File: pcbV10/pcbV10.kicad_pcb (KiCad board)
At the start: 2 copper layers, 100 x 100 mm, 146 parts, among them J1 PROG, J10 Fan1, J11 Fan2, J12 VPS, J13 SPK, J14 LoRa, J2 Servo, J3 I2C, J4 1wire, J5 EXT, J6 Power, J7 485, J8 POWER, J9 RGB, K1 G6K-2, K2 G6K-2, K3 G6K-2, Q1 BC817, Q2 BC817, Q3 AO3400A, Q4 BC817, Q5 IRLML6344, Q6 BC817, Q7 IRLML5203, Q8 IRF530, Q9 IRLML6344, SW1 BLUE, SW2 YELLOW, SW3 GREEN, SW4 RED, SW5 WHITE, U1 AMS1117-3.3, U10 SR602, U11 LM358, U12 DS18B20, U13 DS18B20, U14 IPS_240_240, U15 DS18B20, U16 MODULE_STEPDOWN, U17 RFM95W-868S2, U18 MD8002A, U19 BME280, U2 ESP32-WROOM-32, U20 CCS811, U3 CH340K, U4 MS4525DO, U5 INMP441_Module, U6 MAX3485, U7 BME680, U8 IP2721, U9 BH1750_Module, X1 FAN_6024

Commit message: pcb V10 as ordered at JLCPCB
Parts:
- removed D9: 10V, Diode_SMD:D_MiniMELF
- removed JP1: 485_TERM, Connector_PinHeader_2.54mm:PinHeader_1x02_P2.54mm_Vertical
- removed JP2: FAN 5V 24V, Connector_PinHeader_2.54mm:PinHeader_1x03_P2.54mm_Vertical
- removed Q6: BC817, Package_TO_SOT_SMD:SOT-23
- removed Q7: IRLML5203, Package_TO_SOT_SMD:SOT-23
- removed Q8: IRF530, Package_TO_SOT_THT:TO-220-3_Horizontal_TabDown
- removed R28, R29: 1k, Resistor_SMD:R_0603_1608Metric
- removed R30: 220R, Resistor_SMD:R_1206_3216Metric
- added C31: u1, Capacitor_SMD:C_0603_1608Metric, F.Cu at (83.9, 110.5)
- added C32: 10u, Capacitor_SMD:C_1206_3216Metric, F.Cu at (73.7, 99.4)
- added C33: u1, Capacitor_SMD:C_0805_2012Metric, F.Cu at (75.9, 98.9)
- added C34: u1, Capacitor_SMD:C_0603_1608Metric, F.Cu at (82.5, 98.9)
- added C35: u1, Capacitor_SMD:C_0603_1608Metric, F.Cu at (78.6, 102.2)
- added C36: 22u, Capacitor_SMD:C_0805_2012Metric, F.Cu at (71.1, 90.2)
- added C37: 22u, Capacitor_SMD:C_0805_2012Metric, F.Cu at (69.1, 90.2)
- added D16: Schttky, Diode_SMD:D_SMA, F.Cu at (79.8, 77.9)
- added FID1: Fiducial, Fiducial:Fiducial_1mm_Mask2mm, F.Cu at (55.2, 55.1)
- added FID2: Fiducial, Fiducial:Fiducial_1mm_Mask2mm, F.Cu at (120.0, 146.4)
- added IMG1: Speaker, liebler_DRAWINGS:speaker, F.Cu at (98.9, 93.0)
- added IMG2: Augenschutz, liebler_DRAWINGS:augenschutz, F.Cu at (85.6, 86.0)
- added IMG3: HOT, liebler_DRAWINGS:hot, F.Cu at (71.4, 56.3)
- added IMG4: WHS, liebler_DRAWINGS:LOGO_WHS, B.Cu at (119.4, 143.6)
- added IMG5: QR-CODE, liebler_DRAWINGS:QR_CODE_smopla_de, B.Cu at (84.7, 141.5)
- added IMG6: OPEN Hardware, Symbol:OSHW-Logo2_7.3x6mm_SilkScreen, B.Cu at (139.3, 56.6)
- added IMG7: HOT, liebler_DRAWINGS:hot, F.Cu at (127.6, 59.9)
- added IMG8: HOT_BIG, liebler_DRAWINGS:hot_big, B.Cu at (96.3, 87.1)
- added J15: 1B 2A, Connector_Phoenix_MC:PhoenixContact_MCV_1,5_2-G-3.81_1x02_P3.81mm_Vertical, F.Cu at (66.2, 111.0)
- added J16: BME280, Connector_PinSocket_2.54mm:PinSocket_1x06_P2.54mm_Vertical, F.Cu at (62.5, 132.0)
- added J17: CCS811, Connector_PinSocket_2.54mm:PinSocket_1x08_P2.54mm_Vertical, F.Cu at (138.7, 74.3)
- added J18: Barrel_Jack_Switch, Connector_BarrelJack:BarrelJack_Horizontal, F.Cu at (67.2, 60.7)
- added J19: Supply, Connector_PinHeader_2.54mm:PinHeader_2x04_P2.54mm_Vertical, F.Cu at (142.4, 65.3)
- added L1: 47u, Inductor_SMD:L_Abracon_ASPI-0630LR, F.Cu at (79.8, 72.5)
- added L2: 10uH, Inductor_SMD:L_Abracon_ASPI-0630LR, F.Cu at (77.0, 92.7)
- added MK1: ICS-43434, liebler_SEMICONDUCTORS:MIC_ICS-43434, F.Cu at (86.4, 109.9)
- added R41: M1, Resistor_SMD:R_0603_1608Metric, F.Cu at (61.1, 101.1)
- added R42: 2k2, Capacitor_SMD:C_0603_1608Metric, F.Cu at (103.1, 91.4)
- added R43: M1, Resistor_SMD:R_0603_1608Metric, F.Cu at (86.4, 113.0)
- added R44: 1k, Resistor_SMD:R_0603_1608Metric, F.Cu at (119.0, 128.8)
- added R45: 6k8, Resistor_SMD:R_0603_1608Metric, F.Cu at (83.8, 94.5)
- added R46: 39k, Resistor_SMD:R_0603_1608Metric, F.Cu at (82.3, 91.4)
- added R47: k47, Resistor_SMD:R_0603_1608Metric, F.Cu at (83.8, 91.4)
- added SW10: 5V FAN 24V, liebler_MECH:Switch_SS12D00, F.Cu at (62.0, 83.6)
- added SW11: 24V->5V, liebler_MECH:Switch_SS12D00, F.Cu at (69.8, 86.5)
- added SW12: RESET, Button_Switch_SMD:SW_Push_1P1T_NO_6x6mm_H9.5mm, F.Cu at (76.3, 129.9)
- added SW6: TERM ON, liebler_MECH:Switch_SS12D00, F.Cu at (78.0, 108.8)
- added SW7: LED HEATER, liebler_MECH:Switch_SS12D00, F.Cu at (102.0, 113.2)
- added SW8: REL ROT, liebler_MECH:Switch_SS12D00, F.Cu at (106.0, 122.2)
- added SW9: SNS MOV, liebler_MECH:Switch_SS12D00, F.Cu at (93.3, 113.2)
- added U21: BTS462T, Package_TO_SOT_SMD:TO-252-5_TabPin3, F.Cu at (65.7, 75.7)
- C17, C19: footprint Capacitor_SMD:C_0805_2012Metric -> Capacitor_SMD:C_1206_3216Metric
- C2: footprint Capacitor_SMD:C_0805_2012Metric -> Capacitor_SMD:C_0603_1608Metric
- C21: value u1 -> 1u; footprint Capacitor_SMD:C_0603_1608Metric -> Capacitor_SMD:C_1206_3216Metric
- C22: value 10n -> 10u; footprint Capacitor_SMD:C_0603_1608Metric -> Capacitor_SMD:C_1206_3216Metric
- D10, D11, D12, D13, D14: footprint liebler_OPTO:LED_PLCC_2835_Handsoldering -> liebler_OPTO:LED_PLCC_2835; moved to F.Cu
- D6, D7, D8: footprint LED_SMD:LED_PLCC_2835 -> liebler_OPTO:LED_PLCC_2835
- J1, J8: footprint Connector_USB:USB_C_Receptacle_HRO_TYPE-C-31-M-12 -> liebler_CONN:USB_C_Receptacle_HRO_TYPE-C-31-M-12_IMPROVED
- J12: footprint Connector_PinSocket_2.54mm:PinSocket_2x25_P2.54mm_Vertical -> Connector_PinHeader_2.54mm:PinHeader_2x25_P2.54mm_Vertical
- J13: footprint Connector_PinHeader_2.54mm:PinHeader_1x02_P2.54mm_Vertical -> Connector_Wire:SolderWire-0.1sqmm_1x02_P3.6mm_D0.4mm_OD1mm
- J14: value LoRa -> LoRa Antenna
- J6: value Power -> 5V 3V GN 24
- J9: value RGB -> GN 5V RGB GN
- R13: value 120R -> K12
- R26: value 22k -> 10k
- R27: value 1k -> 1M
- R31: value k1 -> 51k
- R32: value 1k -> 22R
- R33: value 1R -> R68
- RV1: value 5k -> 1k
- SW1: value BLUE -> BTN BLUE; footprint Button_Switch_SMD:SW_Push_1P1T_NO_CK_PTS125Sx43PSMTR -> liebler_MECH:SW_Push_1P1T_NO_CK_PTS125Sx43PSMTR
- SW3, SW4: footprint Button_Switch_SMD:SW_Push_1P1T_NO_CK_PTS125Sx43PSMTR -> liebler_MECH:SW_Push_1P1T_NO_CK_PTS125Sx43PSMTR
- SW5: value WHITE -> BTN WHITE; footprint Button_Switch_SMD:SW_Push_1P1T_NO_CK_PTS125Sx43PSMTR -> liebler_MECH:SW_Push_1P1T_NO_CK_PTS125Sx43PSMTR
- U11: value LM358 -> MP4420; footprint Package_SO:SO-8_3.9x4.9mm_P1.27mm -> Package_TO_SOT_SMD:TSOT-23-8
- U18, U6: footprint Package_SO:SO-8_3.9x4.9mm_P1.27mm -> Package_SO:SOIC-8_3.9x4.9mm_P1.27mm
- U5: value INMP441_Module -> ZXLD1350; footprint liebler_MODULES:INMP441_Module -> Package_TO_SOT_SMD:SOT-23-5
- U9: moved to F.Cu
- moved R19 66.1 mm to (126.4, 54.5)
- moved D6 62.0 mm to (127.4, 59.1), turned to 90 degrees
- moved U5 45.1 mm to (73.5, 72.5), turned to 270 degrees
- moved R26 34.7 mm to (85.3, 69.6)
- moved U9 34.4 mm to (112.4, 92.5), turned to 270 degrees
- moved C21 28.3 mm to (69.0, 70.9), turned to 0 degrees
- moved R33 24.0 mm to (73.6, 75.6), turned to 180 degrees
- moved R12 22.6 mm to (102.4, 103.6)
- moved R11 22.3 mm to (99.1, 107.2)
- moved D4 22.0 mm to (98.8, 104.6), turned to 90 degrees
- moved R8 18.8 mm to (66.0, 140.0), turned to 270 degrees
- moved R36 17.6 mm to (121.8, 124.5), turned to 90 degrees
- moved D11 16.3 mm to (86.1, 79.6), turned to 270 degrees
- moved R5 15.2 mm to (66.0, 143.1), turned to 90 degrees
- moved J7 14.4 mm to (75.1, 109.1), turned to 90 degrees
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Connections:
- C21 pad 1: +24V -> GND
- C21 pad 2: GND -> +24V
- C22 pad 1: Net-(C22-Pad1) -> GND
- C22 pad 2: Net-(C22-Pad2) -> +24V
- D14 pad 2: +24V -> Net-(D14-Pad2)
- J2 pad 1: 485_DI -> FAN1_DRIVE
- J2 pad 2: FAN1_SENSE -> SERVO2
- R27 pad 1: GND -> +24V
- R27 pad 2: Net-(R26-Pad1) -> Net-(R27-Pad2)
- R31 pad 1: Net-(C22-Pad2) -> Net-(R31-Pad1)
- R31 pad 2: Net-(Q8-Pad1) -> Net-(R31-Pad2)
- R32 pad 1: Net-(C22-Pad1) -> Net-(C35-Pad2)
- R32 pad 2: Net-(Q8-Pad3) -> Net-(R32-Pad2)
- R33 pad 1: Net-(Q8-Pad3) -> +24V
- R33 pad 2: GND -> Net-(D14-Pad2)
- RV1 pad 1: AUDIO -> Net-(R42-Pad2)
- U11 pad 1: Net-(C22-Pad2) -> Net-(U11-Pad1)
- U11 pad 2: Net-(C22-Pad1) -> +24V
- U11 pad 3: Net-(R26-Pad1) -> Net-(C35-Pad1)
- U11 pad 5: (no net) -> Net-(R32-Pad2)
- U11 pad 6: (no net) -> Net-(R27-Pad2)
- U11 pad 7: (no net) -> Net-(C34-Pad2)
- U11 pad 8: +24V -> Net-(R31-Pad2)
- U14 pad 6: SPI_IO1 -> SERVO2
- U17 pad 15: SPI_IO1 -> SERVO2
- U2 pad 14: HEATER -> HEATER_LED
- U2 pad 16: LED_WHITE_P -> I2S_SCK
- U2 pad 26: SPI_IO1 -> SERVO2
- U2 pad 28: FAN1_SENSE -> I2S_WS
- U2 pad 29: ROT_B -> I2S_SD
- U2 pad 6: K3_A1 -> I34
- U2 pad 7: MOVE -> I35
- U5 pad 1: GND -> Net-(L1-Pad2)
- U5 pad 2: 485_DE -> GND
- U5 pad 3: 485_RO -> Net-(R26-Pad1)
- U5 pad 4: 485_DI -> Net-(D14-Pad2)
- U5 pad 5: +3V3 -> +24V
- U8 pad 11: /VBUS -> Net-(R41-Pad2)
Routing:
- net SERVO2: track 0.00 -> 102.0 mm, vias 0 -> 2
- net Net-(D6-Pad1): track 92.1 -> 15.7 mm, vias 1 -> 0
- net 485_DI: track 108.7 -> 37.1 mm, vias 2 -> 0
- net SPI_IO1: track 64.3 -> 0.00 mm
- net +3V3: track 379.2 -> 435.8 mm, vias 4 -> 6
- net +24V: track 217.1 -> 185.5 mm, vias 2 -> 5
- net LED_WHITE_P: track 28.9 -> 57.1 mm
- net +5V: track 419.4 -> 393.1 mm, vias 3 -> 2
- net Net-(C36-Pad1): track 0.00 -> 22.5 mm
- net I35: track 0.00 -> 20.8 mm
- net I2S_SCK: track 0.00 -> 18.0 mm, vias 0 -> 2
- net ROT_B: track 34.3 -> 17.9 mm, vias 2 -> 1
- net HEATER: track 77.4 -> 63.1 mm
- net I2S_SD: track 0.00 -> 14.1 mm
- net FAN1_SENSE: track 68.9 -> 82.6 mm, vias 4 -> 2
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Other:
- board text added: "+"
- board text added: "-"
- board text added: "2021-11-25 klaus.liebler@w-hs.de Wissen, was praktisch zählt!"
- board text added: "24 NC B+"
- board text added: "3V 1W GN 5V"
- board text added: "3V GN SC SD GN"
- board text added: "3V3 GND 5V 5V"
- board text added: "3V3 GND SCL SDA NC NC"
- board text added: "A- B+"
- board text added: "FS F+ GND"
- board text added: "G3S1"
- board text added: "G3S2"
- board text added: "K1"
- board text added: "K2"
- board text added: "K3"
- board text added: "Microphone"
- board text added: "NC F+ F-"
- board text added: "NC GN A-"
- board text added: "Speaker"
- board text added: "TERM: for RS485-Termination LED HEATER: power LED or heating resistor @ io12 REL ROT: K3-A1 or rotary encoder @ io34 SNS MOV: fan1-sense or movement-sensor @ io35 24V->5V: activate 24V-to-5V converter 5V FAN 24V: select 24V or 5V for both fans"
- board text added: "TIME REL!"
- board text added: "USB-C PD 20V / 2A"
- board text added: "USB-C Programming"
- board text removed: "2021-09-04 klaus.liebler@w-hs.de Wissen, was praktisch zählt!"
- board text removed: "A- GN NC"
- board text removed: "B+ NC 24"

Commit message: labathome v11 as ordered @ JLCPCB
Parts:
- removed R40: 4k7, Resistor_SMD:R_0603_1608Metric
- removed R43: M1, Resistor_SMD:R_0603_1608Metric
- added C38: 1u, Capacitor_SMD:C_0603_1608Metric, F.Cu at (67.6, 140.0)
- added C39: u1, Capacitor_SMD:C_0603_1608Metric, F.Cu at (83.9, 110.5)
- added C40: 10u, Capacitor_SMD:C_0805_2012Metric_Pad1.18x1.45mm_HandSolder, B.Cu at (117.2, 65.7)
- added C41: u1, Capacitor_SMD:C_0805_2012Metric_Pad1.18x1.45mm_HandSolder, B.Cu at (117.2, 63.6)
- added DWM1: DWM1000, RF_Module:DWM1000, B.Cu at (105.2, 58.0)
- added IMG9: Augenschutz, liebler_DRAWINGS:qwiic, F.Cu at (67.5, 145.5)
- added J20: FAN5V, Connector_JST:JST_XH_B2B-XH-A_1x02_P2.50mm_Vertical, B.Cu at (54.7, 83.7)
- added J21: QWIIC, Connector_JST:JST_SH_SM04B-SRSS-TB_1x04-1MP_P1.00mm_Horizontal, F.Cu at (57.3, 139.3)
- added R28: 4k7, Resistor_SMD:R_0603_1608Metric, F.Cu at (66.2, 132.0)
- added R29: M1, Resistor_SMD:R_0603_1608Metric, F.Cu at (86.4, 113.0)
- added U22: SR602, liebler_MODULES:PIR_Sensor_SR602, F.Cu at (100.0, 67.0)
- C11, C13: footprint Capacitor_SMD:C_0603_1608Metric -> Capacitor_SMD:C_0805_2012Metric_Pad1.18x1.45mm_HandSolder; moved to B.Cu
- C30: value 1u -> u1
- D16: value Schttky -> D
- IMG2: footprint liebler_DRAWINGS:augenschutz -> liebler_DRAWINGS:googles
- J18: value Barrel_Jack_Switch -> Power
- JP3, JP4: value 1I2C_3SPI -> SPI-I2C
- L1: value 47u -> 68u
- R30: renamed from R42; footprint Capacitor_SMD:C_0603_1608Metric -> Resistor_SMD:R_0603_1608Metric
- R37: value 2k2 -> 2k2?
- R38, R39: footprint Capacitor_SMD:C_0603_1608Metric -> Resistor_SMD:R_0603_1608Metric
- SW11: value 24V->5V -> ON 24V->5V
- U1: value AMS1117-3.3 -> AMS1117
- U10: value SR602 -> MS4525DO; footprint liebler_MODULES:PIR_Sensor_SR602 -> liebler_MODULES:MS4525DO
- U12: value DS18B20 -> BME680; footprint Package_TO_SOT_THT:TO-92_HandSolder -> Package_LGA:Bosch_LGA-8_3x3mm_P0.8mm_ClockwisePinNumbering; moved to F.Cu
- U13: value DS18B20 -> BME280; footprint Package_TO_SOT_THT:TO-92_HandSolder -> Package_LGA:Bosch_LGA-8_2.5x2.5mm_P0.65mm_ClockwisePinNumbering
- U15: value DS18B20 -> CCS811; footprint Package_TO_SOT_THT:TO-92_HandSolder -> liebler_SEMICONDUCTORS:AMS_LGA-10-1EP_2.7x4mm_P0.6mm
- U19: value BME280 -> DS18B20; footprint Package_LGA:Bosch_LGA-8_2.5x2.5mm_P0.65mm_ClockwisePinNumbering -> Package_TO_SOT_THT:TO-92_HandSolder; moved to B.Cu
- U20: value CCS811 -> BH1750_Module; footprint liebler_SEMICONDUCTORS:AMS_LGA-10-1EP_2.7x4mm_P0.6mm -> liebler_MODULES:GY-302
- U4: value MS4525DO -> CH340C; footprint liebler_MODULES:MS4525DO -> Package_SO:SOIC-16_3.9x9.9mm_P1.27mm; moved to B.Cu
- U7: value BME680 -> DS18B20; footprint Package_LGA:Bosch_LGA-8_3x3mm_P0.8mm_ClockwisePinNumbering -> Package_TO_SOT_THT:TO-92_HandSolder
- U9: value BH1750_Module -> DS18B20; footprint liebler_MODULES:GY-302 -> Package_TO_SOT_THT:TO-92_HandSolder
- moved C15 100.3 mm to (72.7, 138.0), turned to 90 degrees
- moved U4 98.0 mm to (71.0, 128.4), turned to 270 degrees
- moved U12 86.7 mm to (70.0, 135.8), turned to 90 degrees
- moved U15 85.5 mm to (66.7, 136.2), turned to 0 degrees
- moved U19 84.0 mm to (124.5, 68.3), turned to 270 degrees
- moved C31 71.6 mm to (130.7, 56.3)
- moved U20 63.2 mm to (112.4, 92.5), turned to 270 degrees
- moved U7 56.8 mm to (125.7, 124.5)
- moved U13 53.3 mm to (73.5, 135.1)
- moved IMG5 45.4 mm to (75.9, 96.9)
- moved U10 40.2 mm to (139.2, 58.0)
- moved IMG4 39.8 mm to (129.7, 105.2), turned to 270 degrees
- moved U9 25.0 mm to (118.7, 68.3)
- moved IMG8 18.8 mm to (81.8, 75.2)
- moved C11 16.0 mm to (71.4, 123.6), turned to 180 degrees
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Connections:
- net Net-(C35-Pad1) renamed /psu/SW
- net Net-(D10-Pad1) renamed /D10_COOL
- net Net-(D10-Pad2) renamed /D12_COOL
- net Net-(D11-Pad1) renamed /D11_COOL
- net Net-(D12-Pad2) renamed /D14_COOL
- net Net-(D13-Pad1) renamed /D13_COOL
- C11 pad 2: +3V3 -> Net-(C11-Pad2)
- C13 pad 1: GND -> +5V
- C13 pad 2: +3V3 -> GND
- C15 pad 2: +5V -> +3V3
- C30 pad 1: +3V3 -> GND
- C30 pad 2: GND -> +3V3
- C31 pad 2: +3V3 -> +5V
- J1 pad A6: Net-(J1-PadA6) -> /UD+
- J1 pad A7: Net-(J1-PadA7) -> /UD-
- J1 pad B6: Net-(J1-PadA6) -> /UD+
- J1 pad B7: Net-(J1-PadA7) -> /UD-
- U10 pad 2: +3V3 -> +5V
- U10 pad 3: MOVE -> SDA
- U12 pad 2: 1wire -> +3V3
- U12 pad 3: +3V3 -> SDA
- U13 pad 2: 1wire -> +3V3
- U13 pad 3: +3V3 -> SDA
- U15 pad 2: 1wire -> Net-(R28-Pad1)
- U15 pad 3: +3V3 -> Net-(U15-Pad3)
- U19 pad 1: Net-(U19-Pad1) -> GND
- U19 pad 2: +3V3 -> 1wire
- U19 pad 3: SDA -> +3V3
- U2 pad 16: I2S_SCK -> I2S_WS
- U2 pad 28: I2S_WS -> I2S_SD
- U2 pad 29: I2S_SD -> I2S_SCK
- U20 pad 1: GND -> +3V3
- U20 pad 2: Net-(R40-Pad1) -> GND
- U20 pad 3: Net-(U20-Pad3) -> SCL
- U20 pad 4: Net-(U20-Pad4) -> SDA
- U20 pad 5: Net-(U20-Pad4) -> GND
- U3 pad 1: Net-(J1-PadA6) -> /UD+
- U3 pad 2: Net-(J1-PadA7) -> /UD-
- U4 pad 2: +5V -> PROG_TX
- U4 pad 3: SDA -> PROG_RX
- U4 pad 4: SCL -> Net-(C11-Pad2)
- U4 pad 5: Net-(U4-Pad5) -> /UD+
- U4 pad 6: Net-(U4-Pad6) -> /UD-
- U7 pad 2: +3V3 -> 1wire
- U7 pad 3: SDA -> +3V3
- U9 pad 1: +3V3 -> GND
- U9 pad 2: GND -> 1wire
- U9 pad 3: SCL -> +3V3
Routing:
- net GND: track 63.2 -> 98.2 mm, vias 167 -> 160
- net /UD-: track 0.00 -> 24.5 mm, vias 0 -> 1
- net /UD+: track 0.00 -> 23.9 mm, vias 0 -> 2
- net +5V: track 393.1 -> 415.7 mm, vias 2 -> 3
- net +3V3: track 435.8 -> 456.9 mm
- net Net-(J1-PadA6): track 10.6 -> 0.00 mm, vias 2 -> 0
- net SPI_MISO: track 88.5 -> 97.5 mm
- net PROG_RX: track 24.2 -> 33.2 mm
- net SDA: track 184.2 -> 192.8 mm
- net Net-(J1-PadA7): track 7.53 -> 0.00 mm
- net /DTR: track 9.66 -> 16.5 mm, vias 0 -> 1
- net /RTS: track 3.18 -> 9.95 mm, vias 0 -> 1
- net Net-(J11-Pad2): track 30.3 -> 23.7 mm
- net SCL: track 168.3 -> 174.4 mm, vias 4 -> 5
- net I2S_WS: track 12.6 -> 18.0 mm, vias 0 -> 2
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- added copper zone on B.Cu, net /D10_COOL
- added copper zone on F.Cu, net /D10_COOL
- added copper zone on B.Cu, net /D11_COOL
- added copper zone on F.Cu, net /D11_COOL
- added copper zone on B.Cu, net /D12_COOL
- added copper zone on F.Cu, net /D12_COOL
- added copper zone on B.Cu, net /D13_COOL
- added copper zone on F.Cu, net /D13_COOL
- added copper zone on B.Cu, net /D14_COOL
- added copper zone on F.Cu, net /D14_COOL
- added copper zone on F.Cu, net /psu/SW
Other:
- board text added: "2021-12-22 Klaus Liebler"
- board text added: "F2 5V"
- board text added: "G5S1"
- board text added: "G5S2"
- board text added: "Micro"
- board text added: "TERM: for RS485-Termination LED HEATER: power LED or heating-R@ io12 REL ROT: K3-A1 or rotary encoder @ io34 SNS MOV: fan1- or movem.-sensor @ io35 24V->5V: activate 24V-to-5V converter 5V FAN 24V: select 24V or 5V for both fans"
- board text added: "für K., J. & S."
- board text added: "lab@home 11"
- board text removed: "-F2 +F2 NC"
- board text removed: "2021-11-25 klaus.liebler@w-hs.de Wissen, was praktisch zählt!"
- board text removed: "G3S1"
- board text removed: "G3S2"
- board text removed: "Microphone"
- board text removed: "TERM: for RS485-Termination LED HEATER: power LED or heating resistor @ io12 REL ROT: K3-A1 or rotary encoder @ io34 SNS MOV: fan1-sense or movement-sensor @ io35 24V->5V: activate 24V-to-5V converter 5V FAN 24V: select 24V or 5V for both fans"
- board text removed: "lab@home 10"

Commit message: Moved all components to esp-idf components repository
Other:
- board text added: "PullDown für LED Alle 0805 auf 0603-Fähigkeit prüfen Fiducials in Stencil Freistellung für UWB-Modul"

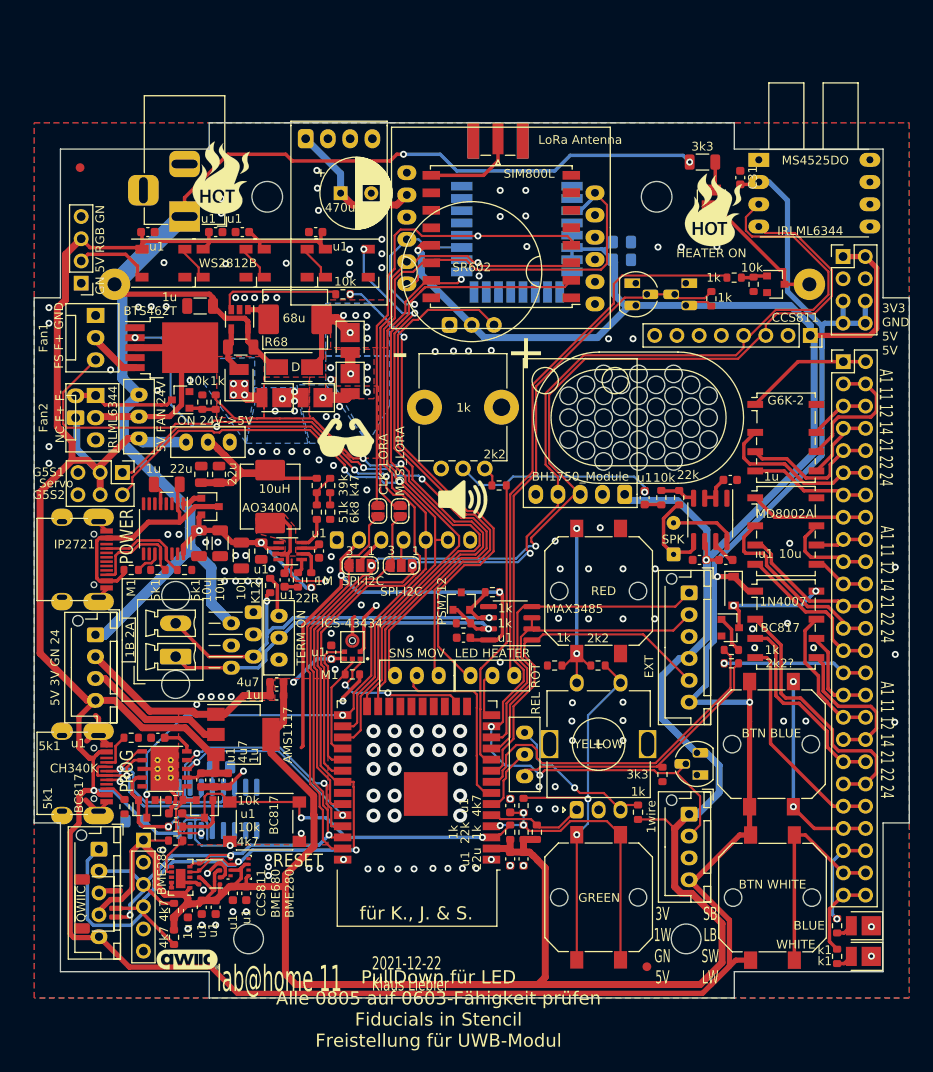
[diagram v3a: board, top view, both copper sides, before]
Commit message: All SMD components orderable @ JLCPCB
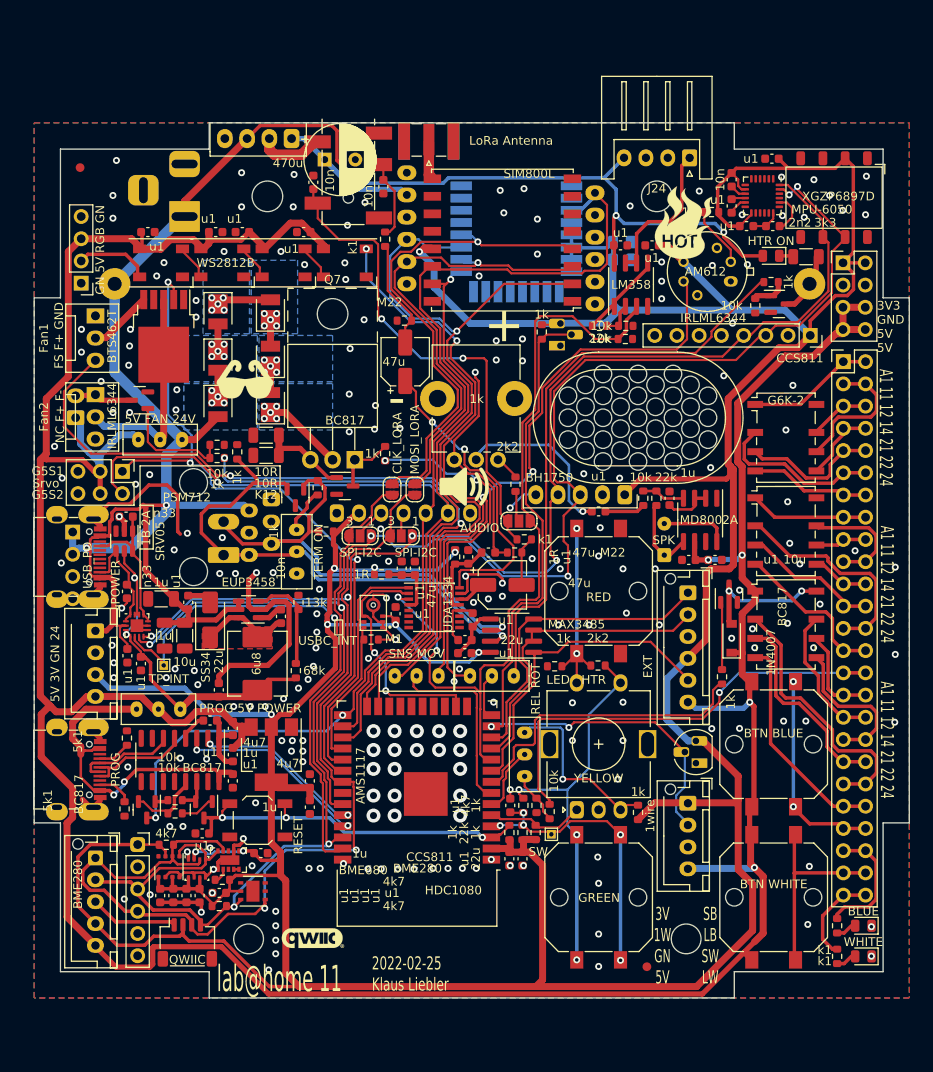
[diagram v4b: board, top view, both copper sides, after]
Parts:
- removed C21: 1u, Capacitor_SMD:C_1206_3216Metric
- removed C34: u1, Capacitor_SMD:C_0603_1608Metric
- removed C37: 22u, Capacitor_SMD:C_0805_2012Metric
- removed IMG3: HOT, liebler_DRAWINGS:hot
- removed L1: 68u, Inductor_SMD:L_Abracon_ASPI-0630LR
- removed MK1: ICS-43434, liebler_SEMICONDUCTORS:MIC_ICS-43434
- removed Q3: AO3400A, Package_TO_SOT_SMD:SOT-23
- removed R10, R9: 5k1, Resistor_SMD:R_0603_1608Metric
- removed R27: 1M, Resistor_SMD:R_0603_1608Metric
- removed R31: 51k, Resistor_SMD:R_0603_1608Metric
- removed R41: M1, Resistor_SMD:R_0603_1608Metric
- removed R47: k47, Resistor_SMD:R_0603_1608Metric
- added C42: u1, Capacitor_SMD:C_0603_1608Metric, F.Cu at (99.6, 99.6)
- added C43: 47u, Capacitor_SMD:C_0603_1608Metric, F.Cu at (101.9, 99.1)
- added C44: u1, Capacitor_SMD:C_0603_1608Metric, F.Cu at (100.1, 106.8)
- added C45: 47u, Capacitor_SMD:CP_Elec_5x5.4, F.Cu at (103.5, 102.8)
- added C46: 47u, Capacitor_SMD:CP_Elec_5x5.4, F.Cu at (92.4, 77.3)
- added C47: 22u, Capacitor_SMD:C_0603_1608Metric, F.Cu at (99.2, 109.1)
- added C48: 10n, Capacitor_SMD:C_0603_1608Metric, F.Cu at (81.9, 56.8)
- added C49: 10n, Capacitor_SMD:C_0603_1608Metric, F.Cu at (89.9, 57.3)
- added C50: 10n, Capacitor_SMD:C_0603_1608Metric, F.Cu at (129.7, 56.5)
- added C51: u1, Capacitor_SMD:C_0603_1608Metric, F.Cu at (129.7, 59.5)
- added C52: u1, Capacitor_SMD:C_0603_1608Metric, F.Cu at (131.4, 61.8)
- added C53: 2n2, Capacitor_SMD:C_0603_1608Metric, F.Cu at (134.4, 61.8)
- added C54: u1, Capacitor_SMD:C_0603_1608Metric, F.Cu at (117.0, 64.0)
- added C55: u1, Capacitor_SMD:C_0603_1608Metric, F.Cu at (120.6, 64.0)
- added C56: n33, Capacitor_SMD:C_0603_1608Metric, F.Cu at (60.5, 95.0)
- added C57: n33, Capacitor_SMD:C_0603_1608Metric, F.Cu at (60.6, 103.5)
- added C58: 1u, Capacitor_SMD:C_1206_3216Metric, F.Cu at (64.5, 104.4)
- added C59: u1, Capacitor_SMD:C_0603_1608Metric, F.Cu at (71.2, 138.0)
- added D9: WHITE, liebler_OPTO:LED_PLCC_2835, F.Cu at (77.0, 82.2)
- added J22: AudioJack3_SwitchT, liebler_CONN:PJ-327A, F.Cu at (85.9, 49.6)
- added J23: USB_PD, Connector_PinHeader_2.54mm:PinHeader_1x04_P2.54mm_Vertical, F.Cu at (54.4, 96.8)
- added J24: AOUT, Connector_JST:JST_XH_S4B-XH-A_1x04_P2.50mm_Horizontal, F.Cu at (124.9, 54.0)
- added JP1: AUDIO, Jumper:SolderJumper-3_P1.3mm_Open_RoundedPad1.0x1.5mm_NumberLabels, F.Cu at (105.4, 95.5)
- added JP2: USBC_INT, liebler_CONN:Jumper_Trace_025x150x015, F.Cu at (84.8, 107.7)
- added Q6: BC817, Package_TO_SOT_SMD:SOT-23, F.Cu at (85.5, 91.5)
- added Q7: TIP41, Package_TO_SOT_THT:TO-220-3_Horizontal_TabUp, F.Cu at (86.6, 88.5)
- added R40: 1R, Resistor_SMD:R_0603_1608Metric, F.Cu at (89.7, 101.6)
- added R42: 1R, Resistor_SMD:R_0603_1608Metric, F.Cu at (98.1, 99.6)
- added R43: M22, Resistor_SMD:R_0603_1608Metric, F.Cu at (104.9, 99.1)
- added R48: M22, Resistor_SMD:R_0603_1608Metric, F.Cu at (92.3, 72.6)
- added R49: k1, Resistor_SMD:R_0603_1608Metric, F.Cu at (106.0, 97.6)
- added R50: k1, Resistor_SMD:R_0603_1608Metric, F.Cu at (90.1, 63.3)
- added R51: 10k, Resistor_SMD:R_0603_1608Metric, F.Cu at (117.6, 73.2)
- added R52: 10k, Resistor_SMD:R_0603_1608Metric, F.Cu at (117.5, 74.7)
- added R53: 22k, Resistor_SMD:R_0603_1608Metric, F.Cu at (114.6, 73.2)
- added R54: 1M, Resistor_SMD:R_0603_1608Metric, F.Cu at (127.4, 60.2)
- added TP1: TP_INT, TestPoint:TestPoint_THTPad_1.0x1.0mm_Drill0.5mm, F.Cu at (64.8, 112.0)
- added TP2: SW, TestPoint:TestPoint_THTPad_1.0x1.0mm_Drill0.5mm, F.Cu at (109.1, 131.3)
- added U23: MPU-6050, Sensor_Motion:InvenSense_QFN-24_4x4mm_P0.5mm, F.Cu at (133.2, 58.4)
- added U24: SRV05, Package_TO_SOT_SMD:SOT-23-6, F.Cu at (60.3, 97.8)
- added X2: XGZP6897D, liebler_MODULES:XGZP6897D, F.Cu at (141.4, 58.5)
- C11: footprint Capacitor_SMD:C_0805_2012Metric_Pad1.18x1.45mm_HandSolder -> Capacitor_SMD:C_0603_1608Metric; moved to F.Cu
- C13: value u1 -> 47u; footprint Capacitor_SMD:C_0805_2012Metric_Pad1.18x1.45mm_HandSolder -> Capacitor_SMD:C_0603_1608Metric; moved to F.Cu
- C19, C32: value 10u -> u1; footprint Capacitor_SMD:C_1206_3216Metric -> Capacitor_SMD:C_0603_1608Metric
- C33, C36: footprint Capacitor_SMD:C_0805_2012Metric -> Capacitor_SMD:C_0603_1608Metric
- C35: value u1 -> 10n
- D16: value D -> SS34
- D6: value HEATER ON -> HTR ON; footprint liebler_OPTO:LED_PLCC_2835 -> LED_SMD:LED_0805_2012Metric
- D7, D8: footprint liebler_OPTO:LED_PLCC_2835 -> Diode_SMD:D_0805_2012Metric
- J2: value Servo -> Srvo
- L2: value 10uH -> 6u8
- R26: value 10k -> 1k
- R32: value 22R -> 10R; footprint Resistor_SMD:R_0603_1608Metric -> Resistor_SMD:R_1206_3216Metric
- R33: value R68 -> 10R
- R36: value 3k3 -> 1k
- R37: value 2k2? -> 10k
- R45: value 6k8 -> 13k
- R46: value 39k -> 68k
- RV1: footprint Potentiometer_THT:Potentiometer_Alps_RK09K_Single_Vertical -> liebler_MECH:Potentiometer_Alps_RK09K_Single_Vertical
- SW11: value ON 24V->5V -> PROG 5V POWER
- SW12: footprint Button_Switch_SMD:SW_Push_1P1T_NO_6x6mm_H9.5mm -> Button_Switch_SMD:SW_SPST_TL3342
- SW7: value LED HEATER -> LED HTR
- U10: value MS4525DO -> LM358; footprint liebler_MODULES:MS4525DO -> Package_SO:SOIC-8_3.9x4.9mm_P1.27mm
- U11: value MP4420 -> FUSB302BMPX; footprint Package_TO_SOT_SMD:TSOT-23-8 -> Package_DFN_QFN:WQFN-14-1EP_2.5x2.5mm_P0.5mm_EP1.45x1.45mm
- U20: value BH1750_Module -> BH1750
- U22: value SR602 -> AM612; footprint liebler_MODULES:PIR_Sensor_SR602 -> liebler_SEMICONDUCTORS:AM612
- U3: value CH340K -> ICS-43432; footprint liebler_SEMICONDUCTORS:SSOP-10_3.9x4.9mm_P1.00mm_EP -> liebler_SEMICONDUCTORS:MIC_ICS-43432
- U4: moved to F.Cu
- U5: value ZXLD1350 -> UDA1334; footprint Package_TO_SOT_SMD:SOT-23-5 -> Package_SO:SSOP-16_4.4x5.2mm_P0.65mm
- U8: value IP2721 -> HDC1080; footprint Package_SO:TSSOP-16_4.4x5mm_P0.65mm -> Package_SON:Texas_PWSON-N6
- U9: value DS18B20 -> EUP3458; footprint Package_TO_SOT_THT:TO-92_HandSolder -> Package_TO_SOT_SMD:SOT-23-6
- moved U9 57.9 mm to (74.5, 105.6), turned to 180 degrees
- moved IMG5 47.5 mm to (33.2, 76.3)
- moved C13 43.1 mm to (93.5, 100.9), turned to -90 degrees
- moved U8 42.7 mm to (75.0, 137.8), turned to 180 degrees
- moved U5 39.7 mm to (95.7, 105.4), turned to 0 degrees
- moved R11 32.4 mm to (73.2, 87.6), turned to 90 degrees
- moved SW11 31.0 mm to (64.2, 117.0), turned to 180 degrees
- moved C11 30.7 mm to (92.0, 100.9), turned to -90 degrees
- moved D16 30.5 mm to (70.1, 106.8), turned to 90 degrees
- moved U3 29.8 mm to (88.8, 106.0), turned to 180 degrees
- moved U22 26.9 mm to (126.9, 67.0)
- moved R37 26.8 mm to (108.9, 128.7), turned to 90 degrees
- moved C36 24.6 mm to (71.1, 114.8)
- moved U10 23.4 mm to (118.2, 68.5), turned to 90 degrees
- moved D4 22.4 mm to (79.8, 92.8), turned to -90 degrees
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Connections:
- C13 pad 1: +5V -> GND
- C13 pad 2: GND -> Net-(C11-Pad2)
- C17 pad 1: GND -> +24V
- C17 pad 2: /VBUS -> GND
- C19 pad 1: +24V -> GND
- C19 pad 2: GND -> /psu/5Vx
- C25 pad 1: +3V3 -> +5V
- C26 pad 1: +3V3 -> +5V
- C31 pad 2: +5V -> +3V3
- C35 pad 1: /psu/SW -> Net-(C35-Pad1)
- C35 pad 2: Net-(C35-Pad2) -> /psu/SW
- C36 pad 1: Net-(C36-Pad1) -> /psu/5Vx
- C6 pad 1: GND -> +5P
- C6 pad 2: +5V -> GND
- D14 pad 2: Net-(D14-Pad2) -> +24V
- D16 pad 1: +24V -> /psu/SW
- D16 pad 2: /D13_COOL -> GND
- D4 pad 1: RS485B -> RS485A
- D4 pad 2: RS485A -> RS485B
- D6 pad 2: Net-(D6-Pad2) -> +24V
- DWM1 pad 1: Net-(DWM1-Pad1) -> unconnected-(DWM1-Pad1)
- DWM1 pad 10: Net-(DWM1-Pad10) -> unconnected-(DWM1-Pad10)
- DWM1 pad 11: Net-(DWM1-Pad11) -> unconnected-(DWM1-Pad11)
- DWM1 pad 12: Net-(DWM1-Pad12) -> unconnected-(DWM1-Pad12)
- DWM1 pad 13: Net-(DWM1-Pad13) -> unconnected-(DWM1-Pad13)
- DWM1 pad 14: Net-(DWM1-Pad14) -> unconnected-(DWM1-Pad14)
- DWM1 pad 15: Net-(DWM1-Pad15) -> unconnected-(DWM1-Pad15)
- DWM1 pad 22: Net-(DWM1-Pad22) -> unconnected-(DWM1-Pad22)
- DWM1 pad 4: Net-(DWM1-Pad4) -> unconnected-(DWM1-Pad4)
- DWM1 pad 9: Net-(DWM1-Pad9) -> unconnected-(DWM1-Pad9)
- GSM_Module1 pad 1: Net-(GSM_Module1-Pad1) -> unconnected-(GSM_Module1-Pad1)
- GSM_Module1 pad 10: Net-(GSM_Module1-Pad10) -> unconnected-(GSM_Module1-Pad10)
- GSM_Module1 pad 11: Net-(GSM_Module1-Pad11) -> unconnected-(GSM_Module1-Pad11)
- GSM_Module1 pad 12: Net-(GSM_Module1-Pad12) -> unconnected-(GSM_Module1-Pad12)
- GSM_Module1 pad 3: Net-(GSM_Module1-Pad3) -> unconnected-(GSM_Module1-Pad3)
- GSM_Module1 pad 8: Net-(GSM_Module1-Pad8) -> unconnected-(GSM_Module1-Pad8)
- GSM_Module1 pad 9: Net-(GSM_Module1-Pad9) -> unconnected-(GSM_Module1-Pad9)
- J1 pad A4: +5V -> +5P
- J1 pad A8: Net-(J1-PadA8) -> unconnected-(J1-PadA8)
- J1 pad A9: +5V -> +5P
- J1 pad B4: +5V -> +5P
- J1 pad B8: Net-(J1-PadB8) -> unconnected-(J1-PadB8)
- J1 pad B9: +5V -> +5P
- J11 pad 3: Net-(J11-Pad3) -> unconnected-(J11-Pad3)
- J16 pad 5: Net-(J16-Pad5) -> unconnected-(J16-Pad5)
- J16 pad 6: Net-(J16-Pad6) -> unconnected-(J16-Pad6)
- J17 pad 6: Net-(J17-Pad6) -> unconnected-(J17-Pad6)
- J17 pad 7: Net-(J17-Pad7) -> unconnected-(J17-Pad7)
- J17 pad 8: Net-(J17-Pad8) -> unconnected-(J17-Pad8)
- J7 pad 1: Net-(J7-Pad1) -> unconnected-(J7-Pad1)
- J7 pad 4: Net-(J7-Pad4) -> unconnected-(J7-Pad4)
- J8 pad A4: /VBUS -> +24V
- J8 pad A5: Net-(J8-PadA5) -> /psu/CC1
- J8 pad A6: Net-(J8-PadA6) -> unconnected-(J8-PadA6)
- J8 pad A7: Net-(J8-PadA7) -> unconnected-(J8-PadA7)
- J8 pad A8: Net-(J8-PadA8) -> unconnected-(J8-PadA8)
- J8 pad A9: /VBUS -> +24V
- J8 pad B4: /VBUS -> +24V
- J8 pad B5: Net-(J8-PadB5) -> /psu/CC2
- J8 pad B6: Net-(J8-PadB6) -> unconnected-(J8-PadB6)
- J8 pad B7: Net-(J8-PadB7) -> unconnected-(J8-PadB7)
- J8 pad B8: Net-(J8-PadB8) -> unconnected-(J8-PadB8)
- J8 pad B9: /VBUS -> +24V
- L2 pad 1: Net-(C36-Pad1) -> /psu/5Vx
- Q5 pad 3: Net-(D6-Pad1) -> Net-(Q5-Pad3)
- R18 pad 2: Net-(D6-Pad1) -> Net-(Q5-Pad3)
- R19 pad 1: +24V -> Net-(D6-Pad1)
- R19 pad 2: Net-(D6-Pad2) -> Net-(Q5-Pad3)
- R26 pad 1: Net-(R26-Pad1) -> Net-(Q6-Pad3)
- R29 pad 1: GND -> I2S_SD
- R29 pad 2: I2S_SD -> GND
- R30 pad 1: AUDIO -> Net-(JP1-Pad2)
- R32 pad 1: Net-(C35-Pad2) -> Net-(Q6-Pad1)
- R32 pad 2: Net-(R32-Pad2) -> GND
- R33 pad 1: +24V -> Net-(Q6-Pad1)
- R33 pad 2: Net-(D14-Pad2) -> GND
- R46 pad 1: Net-(C36-Pad1) -> /psu/5Vx
- R46 pad 2: Net-(R31-Pad1) -> Net-(R45-Pad2)
- SW11 pad 1: +5V -> /psu/5Vx
- SW11 pad 2: Net-(C36-Pad1) -> +5V
- SW11 pad 3: Net-(SW11-Pad3) -> +5P
- SW6 pad 1: Net-(SW6-Pad1) -> unconnected-(SW6-Pad1)
- U10 pad 1: GND -> Net-(R53-Pad1)
- U10 pad 2: +5V -> Net-(R51-Pad2)
- U10 pad 3: SDA -> AUDIO
- U10 pad 4: SCL -> GND
- U10 pad 5: Net-(U10-Pad5) -> Net-(R53-Pad1)
- U10 pad 6: Net-(U10-Pad6) -> Net-(J24-Pad1)
- U10 pad 7: Net-(U10-Pad7) -> Net-(J24-Pad1)
- U10 pad 8: Net-(U10-Pad8) -> +24V
- U11 pad 1: Net-(U11-Pad1) -> /psu/CC2
- U11 pad 3: /psu/SW -> /psu/5Vx
- U11 pad 4: GND -> /psu/5Vx
- U11 pad 5: Net-(R32-Pad2) -> Net-(JP2-Pad2)
- U11 pad 6: Net-(R27-Pad2) -> SCL
- U11 pad 7: Net-(C34-Pad2) -> SDA
- U11 pad 8: Net-(R31-Pad2) -> GND
- U14 pad 7: Net-(U14-Pad7) -> unconnected-(U14-Pad7)
- U15 pad 3: Net-(U15-Pad3) -> unconnected-(U15-Pad3)
- U15 pad 8: Net-(U15-Pad8) -> unconnected-(U15-Pad8)
- U16 pad 2: Net-(U16-Pad2) -> GND
- U16 pad 3: Net-(U16-Pad3) -> +24V
- U16 pad 4: Net-(U16-Pad4) -> unconnected-(U16-Pad4)
- U17 pad 11: Net-(U17-Pad11) -> unconnected-(U17-Pad11)
- U17 pad 12: Net-(U17-Pad12) -> unconnected-(U17-Pad12)
- U17 pad 16: Net-(U17-Pad16) -> unconnected-(U17-Pad16)
- U17 pad 6: Net-(U17-Pad6) -> unconnected-(U17-Pad6)
- U17 pad 7: Net-(U17-Pad7) -> unconnected-(U17-Pad7)
- U18 pad 6: +3V3 -> +5V
- U2 pad 17: Net-(U2-Pad17) -> unconnected-(U2-Pad17)
- U2 pad 18: Net-(U2-Pad18) -> unconnected-(U2-Pad18)
- U2 pad 19: Net-(U2-Pad19) -> unconnected-(U2-Pad19)
- U2 pad 20: Net-(U2-Pad20) -> unconnected-(U2-Pad20)
- U2 pad 21: Net-(U2-Pad21) -> unconnected-(U2-Pad21)
- U2 pad 22: Net-(U2-Pad22) -> unconnected-(U2-Pad22)
- U2 pad 32: Net-(U2-Pad32) -> unconnected-(U2-Pad32)
- U22 pad 2: +3V3 -> Net-(R54-Pad2)
- U22 pad 3: MOVE -> GND
- U3 pad 1: /UD+ -> GND
- U3 pad 2: /UD- -> GND
- U3 pad 3: GND -> +3V3
- U3 pad 4: /DTR -> GND
- U3 pad 5: Net-(U3-Pad5) -> I2S_WS
- U3 pad 6: /RTS -> I2S_SCK
- U3 pad 7: +5V -> I2S_SD
- U4 pad 10: Net-(U4-Pad10) -> unconnected-(U4-Pad10)
- U4 pad 11: Net-(U4-Pad11) -> unconnected-(U4-Pad11)
- U4 pad 12: Net-(U4-Pad12) -> unconnected-(U4-Pad12)
- U4 pad 15: Net-(U4-Pad15) -> unconnected-(U4-Pad15)
- U4 pad 16: +5V -> +5P
- U4 pad 4: Net-(C11-Pad2) -> Net-(C10-Pad1)
- U4 pad 7: Net-(U4-Pad7) -> unconnected-(U4-Pad7)
- U4 pad 8: Net-(U4-Pad8) -> unconnected-(U4-Pad8)
- U4 pad 9: Net-(U4-Pad9) -> unconnected-(U4-Pad9)
- U5 pad 1: Net-(L1-Pad2) -> I2S_SCK
- U5 pad 2: GND -> I2S_WS
- U5 pad 3: Net-(R26-Pad1) -> AUDIO
- U5 pad 4: Net-(D14-Pad2) -> Net-(C11-Pad2)
- U5 pad 5: +24V -> GND
- U8 pad 1: Net-(Q3-Pad1) -> SDA
- U8 pad 2: /VBUS -> GND
- U8 pad 3: (no net) -> unconnected-(U8-Pad3)
- U8 pad 4: (no net) -> unconnected-(U8-Pad4)
- U8 pad 5: GND -> +3V3
- U8 pad 6: (no net) -> SCL
- U8 pad 7: (no net) -> unconnected-(U8-Pad7)
- U9 pad 1: GND -> Net-(C35-Pad1)
- U9 pad 2: 1wire -> GND
- U9 pad 3: +3V3 -> Net-(R45-Pad2)
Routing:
- net +3V3: track 456.9 -> 538.1 mm, vias 6 -> 10
- net GND: track 98.2 -> 162.8 mm, vias 160 -> 217
- net AUDIO: track 33.5 -> 90.9 mm, vias 0 -> 2
- net /analog_amp/LEFT: track 0.00 -> 55.5 mm, vias 0 -> 2
- net SCL: track 174.4 -> 218.5 mm, vias 5 -> 8
- net +5V: track 415.7 -> 373.4 mm, vias 3 -> 4
- net /psu/5Vx: track 0.00 -> 41.1 mm, vias 0 -> 2
- net +5P: track 0.00 -> 38.7 mm, vias 0 -> 2
- net Net-(C46-Pad1): track 0.00 -> 35.1 mm, vias 0 -> 2
- net SDA: track 192.8 -> 227.6 mm, vias 4 -> 6
- net +24V: track 185.5 -> 219.9 mm
- net Net-(J12-Pad29): track 16.6 -> 50.3 mm
- net Net-(JP2-Pad2): track 0.00 -> 31.1 mm, vias 0 -> 1
- net /VBUS: track 28.4 -> 0.00 mm
- net K3_A1: track 31.6 -> 5.93 mm
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- added copper zone on B.Cu, net /D9_COOL
- removed copper zone on F.Cu, net +3V3
- removed copper zone on F.Cu, net /D10_COOL
- removed copper zone on F.Cu, net /D11_COOL
- removed copper zone on F.Cu, net /D12_COOL
- removed copper zone on F.Cu, net /D13_COOL
- removed copper zone on F.Cu, net /D14_COOL
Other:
- net class Default removed
- board text added: "2022-02-25 Klaus Liebler"
- board text added: "OUT GND GND 24V"
- board text added: "S1 5 G"
- board text added: "S2 5 G"
- board text removed: "2021-12-22 Klaus Liebler"
- board text removed: "PullDown für LED Alle 0805 auf 0603-Fähigkeit prüfen Fiducials in Stencil Freistellung für UWB-Modul"
- board text removed: "S1 5V GN"
- board text removed: "S2 5V GN"
- board text removed: "für K., J. & S."
